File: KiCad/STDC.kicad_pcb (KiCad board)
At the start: 4 copper layers, 38 x 48 mm, 126 parts, among them IC1 TPS22916CNYFPR, IC2 TPS22916CNYFPR, IC3 R1200N001A-TR-FE, IC4 MS5849-30BA, IC5 W25Q32JWSNIQ, J1 TC2030, J2 Conn_01x03_BATT, J3 Conn_01x34_NHD_18, Q1 AO3400A, Q2 AO3400A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

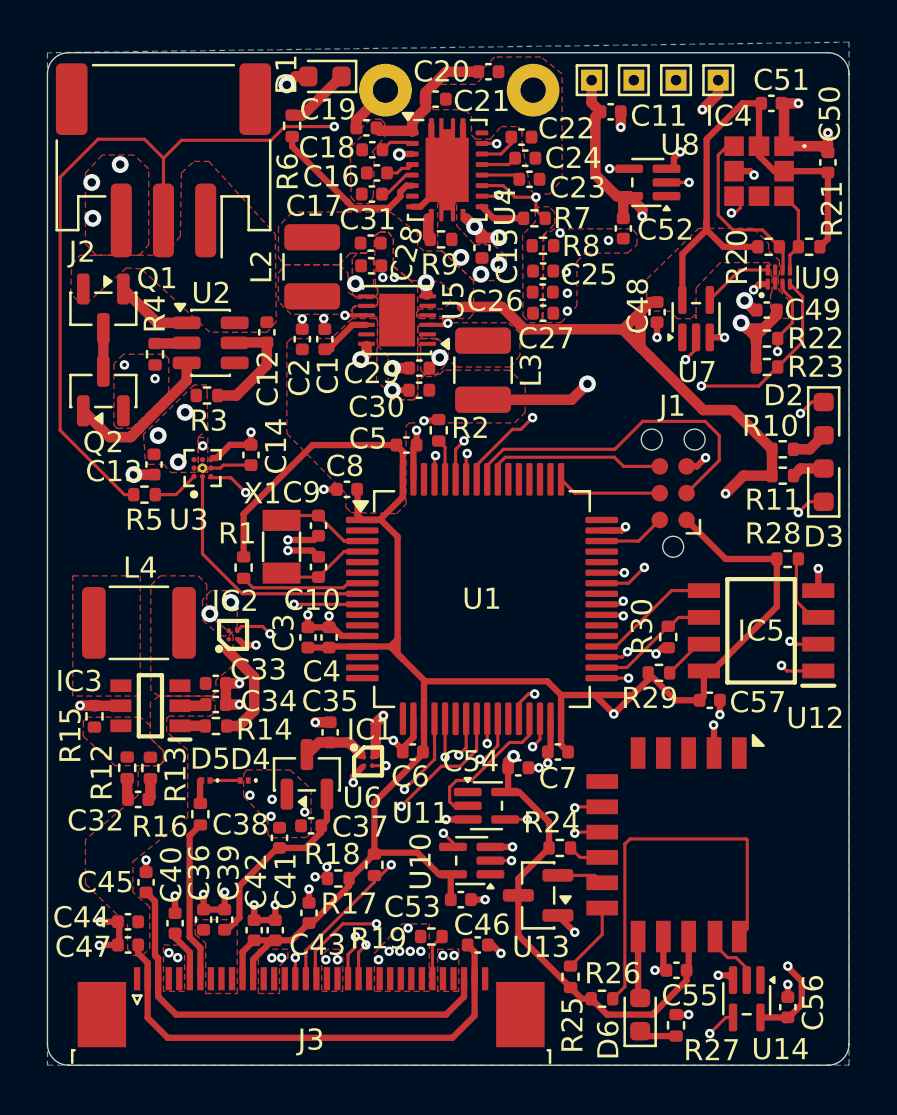
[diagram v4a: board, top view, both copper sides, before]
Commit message: Display VCC more space
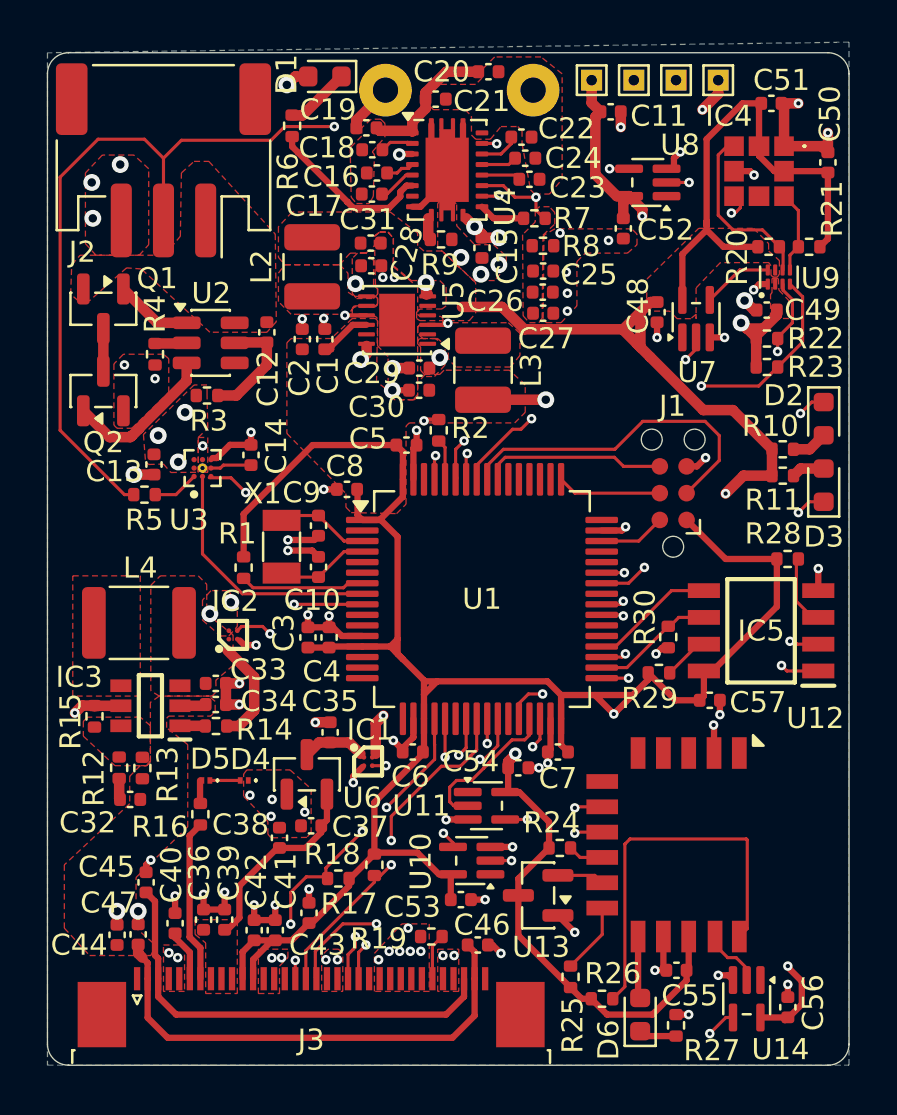
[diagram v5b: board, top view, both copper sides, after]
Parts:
- added G***: LOGO, images:eth_logo_neg, B.Cu at (144.6, 122.9)
- moved C44 0.81 mm to (128.3, 142.3), turned to 90 degrees
- moved C47 0.69 mm to (129.3, 142.3), turned to 90 degrees
- moved C32 0.38 mm to (128.9, 135.9)
- moved R12 0.38 mm to (128.4, 134.4)
- moved R13 0.38 mm to (129.5, 134.4)
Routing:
- net GND: track 76.3 -> 75.2 mm
- net +3.3V: track 101.7 -> 102.7 mm
- net DISPLAY_VCC: track 25.7 -> 24.7 mm
- net +1V8: track 151.2 -> 152.1 mm
- net /BLE_TX_IND: track 25.7 -> 26.3 mm
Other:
- board text added: "STDC v1"
- board text added: "Sebastian Thomas 03/2026"

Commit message: Wider power traces
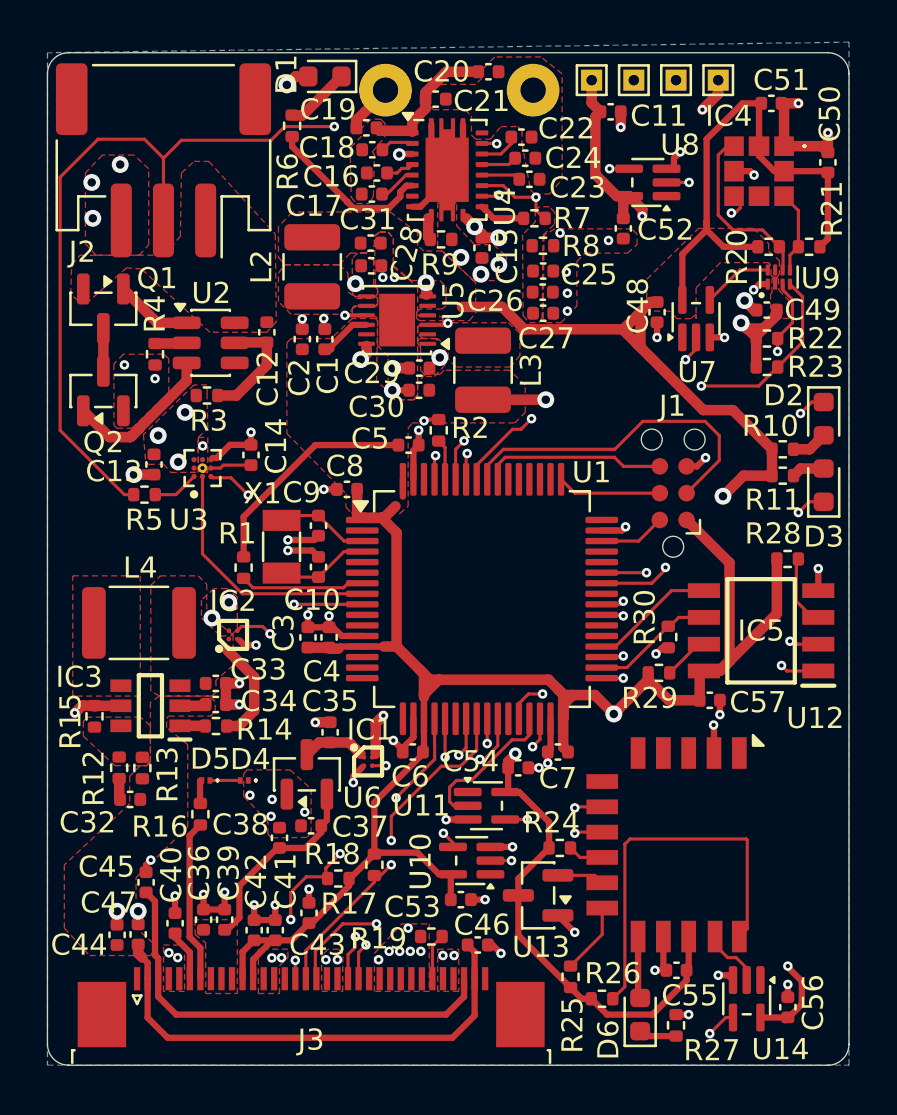
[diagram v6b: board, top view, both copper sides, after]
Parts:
- moved C5 0.10 mm to (142.1, 119.1)
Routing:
- net +1V8: track 152.1 -> 151.4 mm

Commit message: Move Logo
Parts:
- moved G*** 0.22 mm to (144.5, 122.7)
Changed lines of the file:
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@@
 	(footprint "images:eth_logo_neg"
 		(layer "B.Cu")
-		(at 144.630529 122.863044 180)
+		(at 144.530529 122.663044 180)
 		(property "Reference" "G***"
 			(at 0 0 0)
@@
 	)
 	(gr_text "Sebastian Thomas\n03/2026"
-		(at 145.2 128.9 0)
+		(at 145.1 128.7 0)
 		(layer "B.SilkS")
 		(effects
@@
 	)
 	(gr_text "STDC v1"
-		(at 151.2 127.2 0)
+		(at 151.1 127 0)
 		(layer "B.SilkS")
 		(effects

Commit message: Polarity Silkscreen
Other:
- board text added: "+"
- board text added: "-"
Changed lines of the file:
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@@
 		(tags "inductor")
 		(property "Reference" "L2"
-			(at 0 -2.4 90)
+			(at -0.55 -2.25 90)
 			(layer "F.SilkS")
 			(effects
@@
 		(tags "SOT TO_SOT_SMD")
 		(property "Reference" "U2"
-			(at 0.0275 -2.35 180)
+			(at -0.0375 -2.3542 180)
 			(layer "F.SilkS")
 			(effects
@@
 		(tags "connector JST PH horizontal")
 		(property "Reference" "J2"
-			(at 3.85 -4.35 180)
+			(at 0 -5.7 180)
 			(layer "F.SilkS")
 			(effects
@@
 		(tags "SOT TO_SOT_SMD")
 		(property "Reference" "Q1"
-			(at -1.4375 -2.55 0)
+			(at 1.6625 1.35 0)
 			(layer "F.SilkS")
 			(effects
@@
 		(layer "Edge.Cuts")
 	)
+	(gr_text "-"
+		(at 133.4 110.4 0)
+		(layer "F.SilkS")
+		(effects
+			(font
+				(size 1 1)
+				(thickness 0.153)
+			)
+			(justify left bottom)
+		)
+	)
+	(gr_text "+"
+		(at 126.2 110.4 0)
+		(layer "F.SilkS")
+		(effects
+			(font
+				(size 1 1)
+				(thickness 0.153)
+			)
+			(justify left bottom)
+		)
+	)
 	(gr_text "Sebastian Thomas\n03/2026"
 		(at 145.1 128.7 0)
@@
 		)
 	)
+	(group ""
+		(members "2981ea19-ab3d-4aff-a8a0-b4612068c266" "39f45599-4ece-4f4a-9360-bf556c94d443"
+			"4d0a6bda-07c3-4eeb-819e-60e50a9e25d1" "501cba35-c188-453d-9dfd-82877e33c1eb"
+			"62923fd2-cc42-4087-83f1-8d8420c0c642" "6360ea8d-7601-4fc5-b050-87efd0585772"
+			"660b09ba-0841-42cb-b19b-350961d329ff" "887ebf71-8d8b-4129-8d78-52e133b28110"
+			"96d22747-7180-4a4f-a338-cece32fb6234" "9874394b-2491-4e99-8a01-15c11e8ebd58"
+			"b6153898-97dd-47a8-baa3-70c93a0d39fd" "c1d59b6a-c1b5-4e36-b4f6-315e3d7c4760"
+			"f80e10ce-d404-4d1c-9ad4-b19dc3e0b497"
+		)
+	)
